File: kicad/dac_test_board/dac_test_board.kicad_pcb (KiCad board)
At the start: 2 copper layers, 44.7 x 44.6 mm, 29 parts, among them J10 Data_In, J2 Vcca_select, J3 Data_Out, J7 Vccb_select, U2 SN74LVC8T245

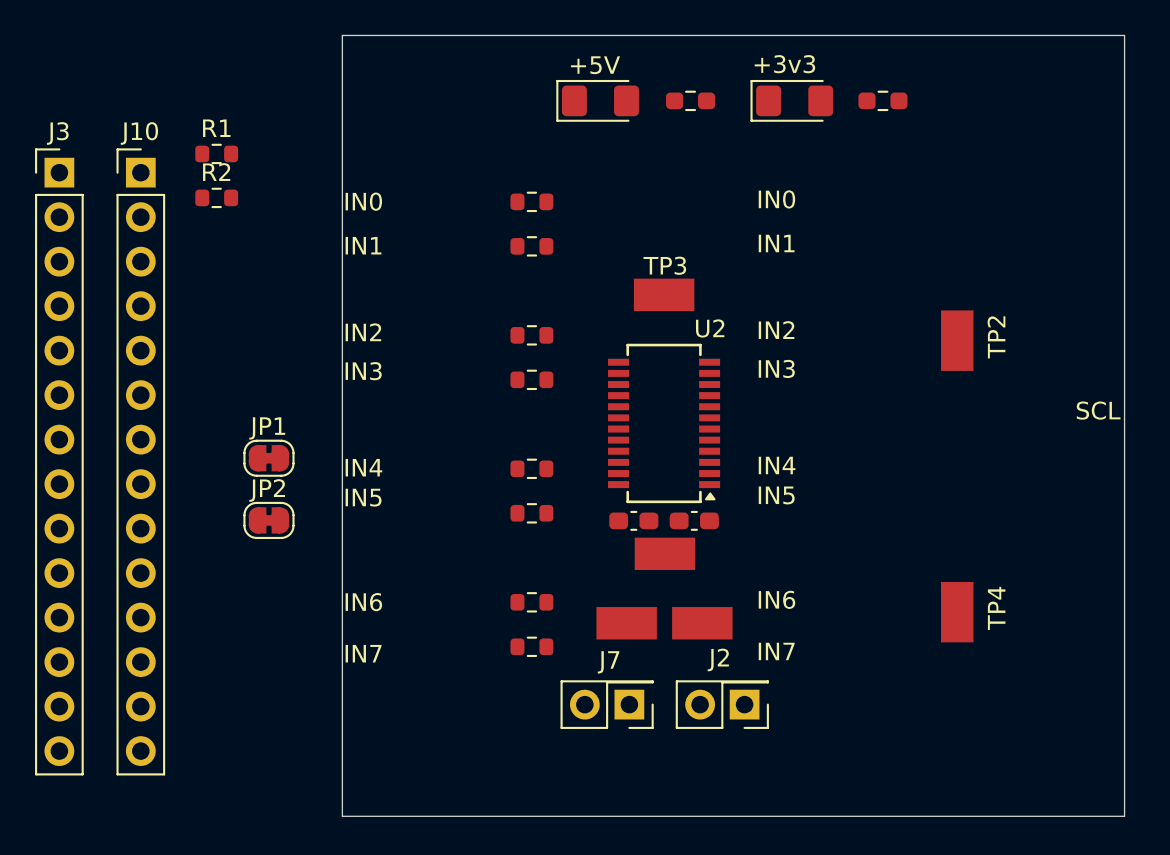
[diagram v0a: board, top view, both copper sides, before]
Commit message: renamed files, was working on wrong directory
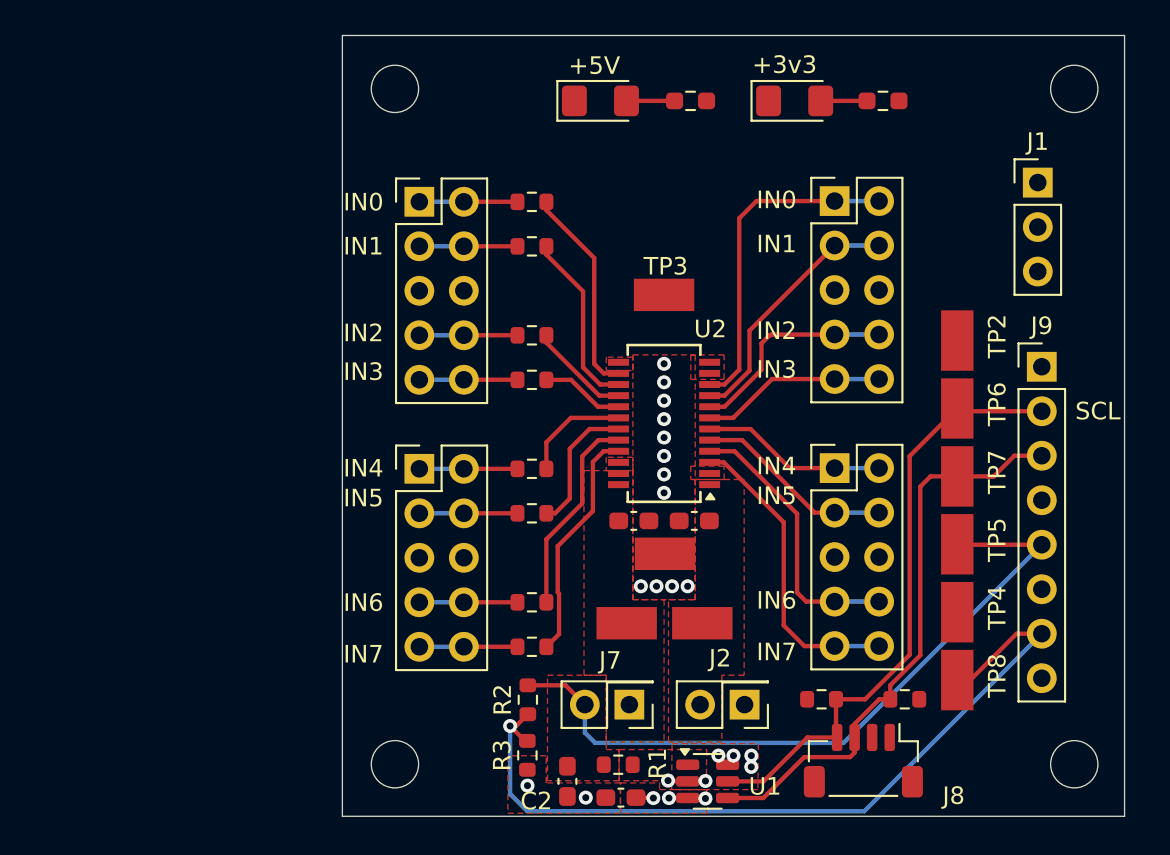
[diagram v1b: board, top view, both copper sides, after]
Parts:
- removed J10: Data_In, Connector_PinHeader_2.54mm:PinHeader_1x14_P2.54mm_Vertical
- removed JP1, JP2: Jumper_2_Bridged, Jumper:SolderJumper-2_P1.3mm_Bridged_RoundedPad1.0x1.5mm
- added C1: 1u, Capacitor_SMD:C_0603_1608Metric_Pad1.08x0.95mm_HandSolder, F.Cu at (157.6, 119.0)
- added C2: 100n, Capacitor_SMD:C_0603_1608Metric_Pad1.08x0.95mm_HandSolder, F.Cu at (154.5, 118.1)
- added H1: MountingHole, MountingHole:MountingHole_2.7mm, F.Cu at (183.4, 78.5)
- added H2: MountingHole, MountingHole:MountingHole_2.7mm, F.Cu at (183.4, 117.1)
- added H3: MountingHole, MountingHole:MountingHole_2.7mm, F.Cu at (144.7, 78.5)
- added H4: MountingHole, MountingHole:MountingHole_2.7mm, F.Cu at (144.7, 117.1)
- added J1: Power, Connector_PinHeader_2.54mm:PinHeader_1x03_P2.54mm_Vertical, F.Cu at (181.4, 83.9)
- added J4: In_Lo, Connector_PinHeader_2.54mm:PinHeader_2x05_P2.54mm_Vertical, F.Cu at (146.1, 85.0)
- added J5: Out_Hi, Connector_PinHeader_2.54mm:PinHeader_2x05_P2.54mm_Vertical, F.Cu at (169.8, 100.2)
- added J6: Out_Lo, Connector_PinHeader_2.54mm:PinHeader_2x05_P2.54mm_Vertical, F.Cu at (169.8, 84.9)
- added J8: JST_SH_BM04B-SRSS-TB, Connector_JST:JST_SH_BM04B-SRSS-TB_1x04-1MP_P1.00mm_Vertical, F.Cu at (171.4, 116.9)
- added J9: Signals, Connector_PinHeader_2.54mm:PinHeader_1x08_P2.54mm_Vertical, F.Cu at (181.6, 94.4)
- added R12: 10k, Resistor_SMD:R_0603_1608Metric, F.Cu at (169.0, 113.4)
- added R13: 10k, Resistor_SMD:R_0603_1608Metric, F.Cu at (173.8, 113.4)
- added R3: 10k, Resistor_SMD:R_0603_1608Metric, F.Cu at (152.2, 116.6)
- added TP5: TestPoint_Harwin, My Libraries:Harwin-S1751-46-Test-Point, F.Cu at (176.8, 104.5)
- added TP6: TestPoint_Harwin, My Libraries:Harwin-S1751-46-Test-Point, F.Cu at (176.8, 96.8)
- added TP7: TestPoint_Harwin, My Libraries:Harwin-S1751-46-Test-Point, F.Cu at (176.8, 100.7)
- added TP8: TestPoint_Harwin, My Libraries:Harwin-S1751-46-Test-Point, F.Cu at (176.8, 112.3)
- added U1: MCP4725A2T-E/CH, Package_TO_SOT_SMD:SOT-23-6, F.Cu at (162.5, 118.1)
- D1: value Vb -> 5V
- D2: value Va -> 3v3
- J3: value Data_Out -> In_Hi; footprint Connector_PinHeader_2.54mm:PinHeader_1x14_P2.54mm_Vertical -> Connector_PinHeader_2.54mm:PinHeader_2x05_P2.54mm_Vertical
- R1: value 1k -> 0
- R2: value 1k -> 10k
- moved R1 41.7 mm to (157.4, 117.1), turned to 180 degrees
- moved R2 33.7 mm to (152.2, 113.4), turned to 90 degrees
- moved J3 26.6 mm to (146.1, 100.2)
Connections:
- J2 pad 1: /Va_In -> +3V3
- J3 pad 1: /Va_In -> /IN04
- J3 pad 10: /BUF03 -> /IN07
- J3 pad 2: GND -> /IN04
- J3 pad 3: /DIR -> /IN05
- J3 pad 4: GND -> /IN05
- J3 pad 5: /BUF07 -> GND
- J3 pad 6: /BUF06 -> GND
- J3 pad 7: /BUF05 -> /IN06
- J3 pad 8: /BUF04 -> /IN06
- J3 pad 9: GND -> /IN07
- J7 pad 2: /Vb_In -> /Vdac_out
- R1 pad 1: /DIR -> Net-(U1-VOUT)
- R1 pad 2: GND -> /Vdac_out
- R14 pad 1: Net-(JP1-A) -> +5V
- R15 pad 1: Net-(JP2-A) -> +3V3
- R2 pad 1: /OE -> /Vdac_half
- R2 pad 2: GND -> /Vdac_out
- U2 pad 2: /DIR -> GND
- U2 pad 22: /OE -> GND
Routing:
- net /Vdac_half: track 0.00 -> 47.4 mm, vias 0 -> 1
- net /Vdac_out: track 0.00 -> 41.2 mm
- net /I2C1_SCL: track 0.00 -> 34.8 mm
- net /I2C1_SDA: track 0.00 -> 33.1 mm
- net /BUF00: track 0.00 -> 19.1 mm
- net /BUF07: track 0.00 -> 17.5 mm
- net /BUF06: track 0.00 -> 15.9 mm
- net /BUF01: track 0.00 -> 14.6 mm
- net /B7: track 0.00 -> 13.4 mm
- net /BUF02: track 0.00 -> 12.3 mm
- net /B0: track 0.00 -> 12.0 mm
- net /B6: track 0.00 -> 11.6 mm
- net /BUF05: track 0.00 -> 11.4 mm
- net /BUF04: track 0.00 -> 10.6 mm
- net /BUF03: track 0.00 -> 10.6 mm
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- added copper zone on F.Cu, net +5V
- added copper zone on F.Cu, net /Vdac_out
- added copper zone on F.Cu, net GND
- added copper zone on In1.Cu, net GND
- added copper zone on F.Cu, net Net-(U1-VOUT)
- added copper zone on F.Cu, net Vcca
- added copper zone on F.Cu, net Vccb
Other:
- copper layers 2 -> 4

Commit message: schematic passes erc
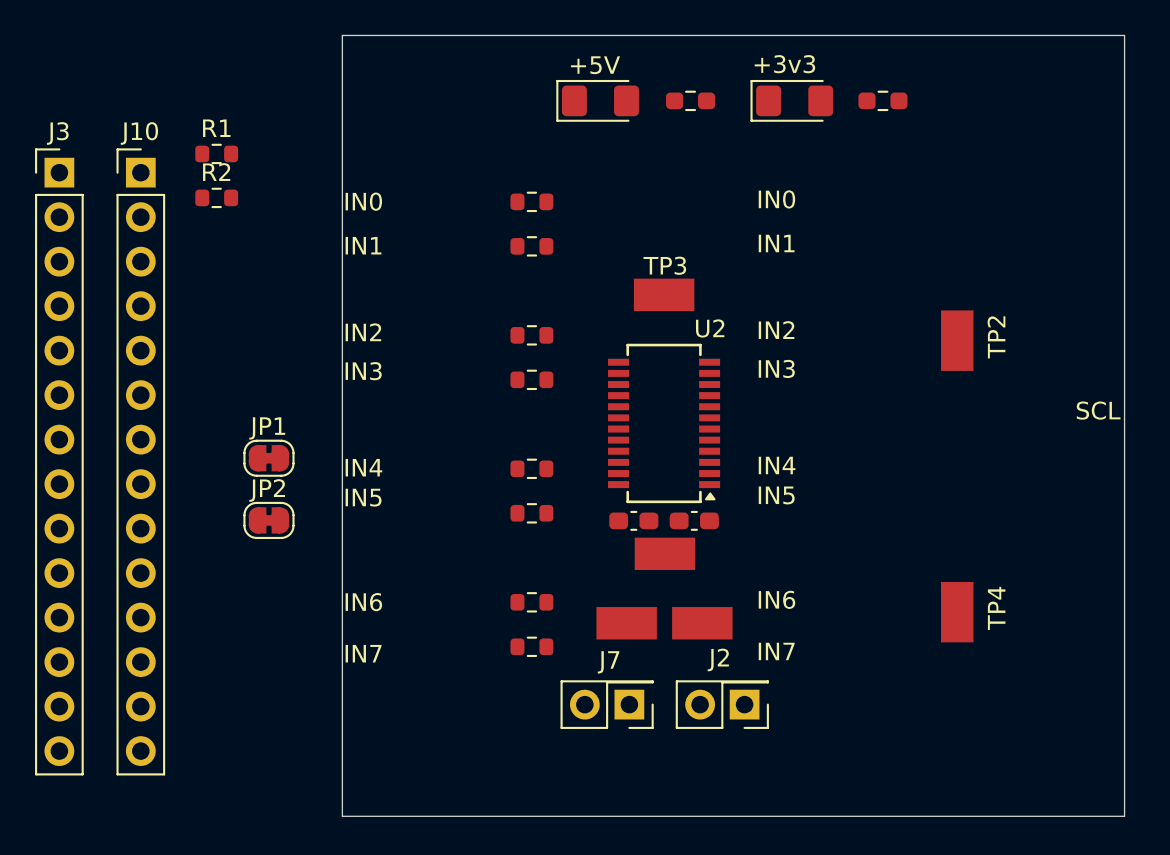
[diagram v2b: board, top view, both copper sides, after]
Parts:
- removed C1: 1u, Capacitor_SMD:C_0603_1608Metric_Pad1.08x0.95mm_HandSolder
- removed C2: 100n, Capacitor_SMD:C_0603_1608Metric_Pad1.08x0.95mm_HandSolder
- removed H1, H2, H3, H4: MountingHole, MountingHole:MountingHole_2.7mm
- removed J1: Power, Connector_PinHeader_2.54mm:PinHeader_1x03_P2.54mm_Vertical
- removed J4: In_Lo, Connector_PinHeader_2.54mm:PinHeader_2x05_P2.54mm_Vertical
- removed J5: Out_Hi, Connector_PinHeader_2.54mm:PinHeader_2x05_P2.54mm_Vertical
- removed J6: Out_Lo, Connector_PinHeader_2.54mm:PinHeader_2x05_P2.54mm_Vertical
- removed J8: JST_SH_BM04B-SRSS-TB, Connector_JST:JST_SH_BM04B-SRSS-TB_1x04-1MP_P1.00mm_Vertical
- removed J9: Signals, Connector_PinHeader_2.54mm:PinHeader_1x08_P2.54mm_Vertical
- removed R12, R13, R3: 10k, Resistor_SMD:R_0603_1608Metric
- removed TP5, TP6, TP7, TP8: TestPoint_Harwin, My Libraries:Harwin-S1751-46-Test-Point
- removed U1: MCP4725A2T-E/CH, Package_TO_SOT_SMD:SOT-23-6
- added J10: Data_In, Connector_PinHeader_2.54mm:PinHeader_1x14_P2.54mm_Vertical, F.Cu at (130.1, 83.3)
- added JP1: Jumper_2_Bridged, Jumper:SolderJumper-2_P1.3mm_Bridged_RoundedPad1.0x1.5mm, F.Cu at (137.5, 99.6)
- added JP2: Jumper_2_Bridged, Jumper:SolderJumper-2_P1.3mm_Bridged_RoundedPad1.0x1.5mm, F.Cu at (137.5, 103.2)
- D1: value 5V -> Vb
- D2: value 3v3 -> Va
- J3: value In_Hi -> Data_Out; footprint Connector_PinHeader_2.54mm:PinHeader_2x05_P2.54mm_Vertical -> Connector_PinHeader_2.54mm:PinHeader_1x14_P2.54mm_Vertical
- R1: value 0 -> 1k
- R2: value 10k -> 1k
- moved R1 41.7 mm to (134.5, 82.3), turned to 0 degrees
- moved R2 33.7 mm to (134.5, 84.8), turned to 0 degrees
- moved J3 26.6 mm to (125.5, 83.3)
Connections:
- J2 pad 1: +3V3 -> /Va_In
- J3 pad 1: /IN04 -> /Va_In
- J3 pad 10: /IN07 -> /BUF03
- J3 pad 2: /IN04 -> GND
- J3 pad 3: /IN05 -> /DIR
- J3 pad 4: /IN05 -> GND
- J3 pad 5: GND -> /BUF07
- J3 pad 6: GND -> /BUF06
- J3 pad 7: /IN06 -> /BUF05
- J3 pad 8: /IN06 -> /BUF04
- J3 pad 9: /IN07 -> GND
- J7 pad 2: /Vdac_out -> /Vb_In
- R1 pad 1: Net-(U1-VOUT) -> /DIR
- R1 pad 2: /Vdac_out -> GND
- R14 pad 1: +5V -> Net-(JP1-A)
- R15 pad 1: +3V3 -> Net-(JP2-A)
- R2 pad 1: /Vdac_half -> /OE
- R2 pad 2: /Vdac_out -> GND
- U2 pad 2: GND -> /DIR
- U2 pad 22: GND -> /OE
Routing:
- net /Vdac_half: track 47.4 -> 0.00 mm, vias 1 -> 0
- net /Vdac_out: track 41.2 -> 0.00 mm
- net /I2C1_SCL: track 34.8 -> 0.00 mm
- net /I2C1_SDA: track 33.1 -> 0.00 mm
- net /BUF00: track 19.1 -> 0.00 mm
- net /BUF07: track 17.5 -> 0.00 mm
- net /BUF06: track 15.9 -> 0.00 mm
- net /BUF01: track 14.6 -> 0.00 mm
- net /B7: track 13.4 -> 0.00 mm
- net /BUF02: track 12.3 -> 0.00 mm
- net /B0: track 12.0 -> 0.00 mm
- net /B6: track 11.6 -> 0.00 mm
- net /BUF05: track 11.4 -> 0.00 mm
- net /BUF04: track 10.6 -> 0.00 mm
- net /BUF03: track 10.6 -> 0.00 mm
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- removed copper zone on F.Cu, net +5V
- removed copper zone on F.Cu, net /Vdac_out
- removed copper zone on F.Cu, net GND
- removed copper zone on In1.Cu, net GND
- removed copper zone on F.Cu, net Net-(U1-VOUT)
- removed copper zone on F.Cu, net Vcca
- removed copper zone on F.Cu, net Vccb
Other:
- copper layers 4 -> 2
